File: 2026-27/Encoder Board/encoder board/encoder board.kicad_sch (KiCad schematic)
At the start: 7 parts, among them J1 jst-ph, U1 TLE5012BE1000

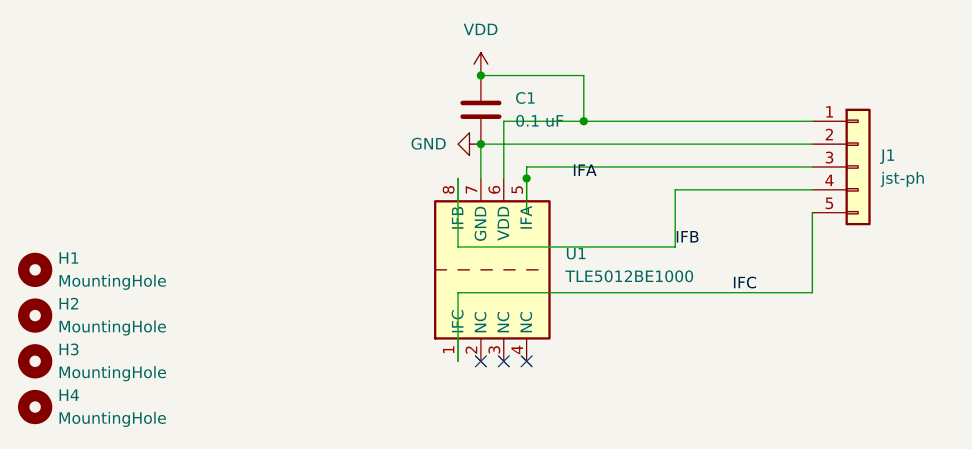
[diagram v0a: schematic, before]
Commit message: encoder board
designed encoder board to mechanical team's size specifications
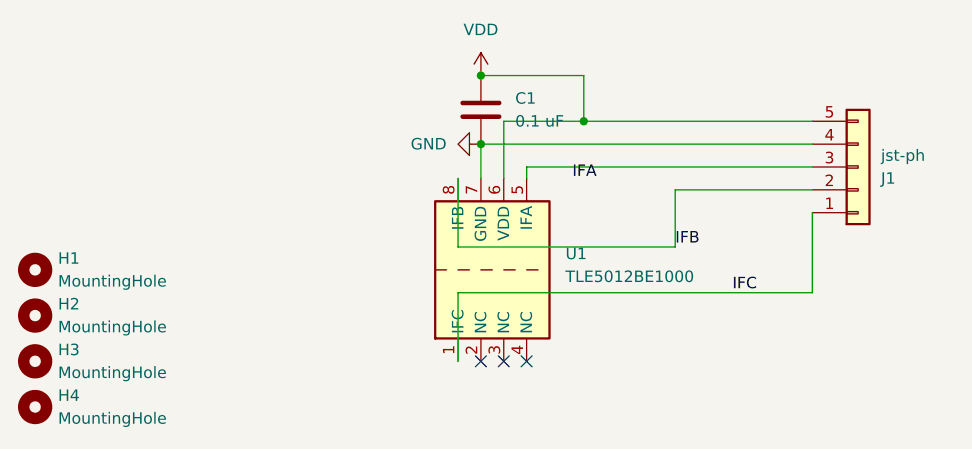
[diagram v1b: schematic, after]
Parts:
- H1, H2, H3, H4: footprint MountingHole:MountingHole_3.2mm_M3 -> MountingHole:MountingHole_2.7mm_M2.5
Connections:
- net GND: now also J1.4 (Pin_4); no longer J1.2 (Pin_2)
- net IFC: now also J1.1 (Pin_1); no longer J1.5 (Pin_5)
- net VDD: now also J1.2 (Pin_2), J1.5 (Pin_5); no longer J1.1 (Pin_1), J1.4 (Pin_4)
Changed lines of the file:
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@@
-		(color 0 0 0 0)
-	)
-	(junction
-		(at 135.89 58.42)
-		(diameter 0)
 		(color 0 0 0 0)
 	)
@@
 	(wire
 		(pts
-			(xy 135.89 58.42) (xy 135.89 57.15)
-		)
-		(stroke
-			(width 0)
-			(type default)
-		)
-	)
-	(wire
-		(pts
 			(xy 142.24 52.07) (xy 133.35 52.07)
 		)
@@
 	(wire
 		(pts
-			(xy 135.89 58.42) (xy 135.89 62.23)
+			(xy 135.89 57.15) (xy 135.89 58.42)
 		)
 		(stroke
@@
 			)
 		)
-		(property "Footprint" "MountingHole:MountingHole_3.2mm_M3"
+		(property "Footprint" "MountingHole:MountingHole_2.7mm_M2.5"
 			(at 81.28 68.58 0)
 			(hide yes)
@@
 	)
 	(symbol
+		(lib_id "Interface_CAN_LIN:ISO1044BD")
+		(at 130.81 68.58 90)
+		(unit 1)
+		(body_style 1)
+		(exclude_from_sim no)
+		(in_bom yes)
+		(on_board yes)
+		(in_pos_files yes)
+		(dnp no)
+		(property "Reference" "U1"
+			(at 140.208 66.802 90)
+			(show_name no)
+			(do_not_autoplace no)
+			(effects
+				(font
+					(size 1.27 1.27)
+				)
+				(justify right)
+			)
+		)
+		(property "Value" "TLE5012BE1000"
+			(at 140.208 69.342 90)
+			(show_name no)
+			(do_not_autoplace no)
+			(effects
+				(font
+					(size 1.27 1.27)
+				)
+				(justify right)
+			)
+		)
+		(property "Footprint" "Package_SO:SOIC-8_3.9x4.9mm_P1.27mm"
+			(at 140.97 68.58 0)
+			(hide yes)
+			(show_name no)
+			(do_not_autoplace no)
+			(effects
+				(font
+					(size 1.27 1.27)
+					(italic yes)
+				)
+			)
+		)
+		(property "Datasheet" "https://www.ti.com/lit/ds/symlink/iso1044.pdf"
+			(at 143.51 68.58 0)
+			(hide yes)
+			(show_name no)
+			(do_not_autoplace no)
+			(effects
+				(font
+					(size 1.27 1.27)
+				)
+			)
+		)
+		(property "Description" "angle sensor, SOIC-8"
+			(at 118.872 67.31 0)
+			(hide yes)
+			(show_name no)
+			(do_not_autoplace no)
+			(effects
+				(font
+					(size 1.27 1.27)
+				)
+			)
+		)
+		(pin "7"
+		)
+		(pin "4"
+		)
+		(pin "6"
+		)
+		(pin "1"
+		)
+		(pin "2"
+		)
+		(pin "8"
+		)
+		(pin "5"
+		)
+		(pin "3"
+		)
+		(instances
+			(project "encoder board"
+				(path "/4ad8da32-6a39-4fcb-82be-0e55f6dd2596"
+					(reference "U1")
+					(unit 1)
+				)
+			)
+		)
+	)
+	(symbol
 		(lib_id "Mechanical:MountingHole")
 		(at 81.28 73.66 0)
@@
 			)
 		)
-		(property "Footprint" "MountingHole:MountingHole_3.2mm_M3"
+		(property "Footprint" "MountingHole:MountingHole_2.7mm_M2.5"
 			(at 81.28 73.66 0)
 			(hide yes)
@@
 			)
 		)
-		(property "Footprint" "MountingHole:MountingHole_3.2mm_M3"
+		(property "Footprint" "MountingHole:MountingHole_2.7mm_M2.5"
 			(at 81.28 83.82 0)
 			(hide yes)
@@
 	)
 	(symbol
-		(lib_id "Connector_Generic:Conn_01x05")
-		(at 172.72 57.15 0)
-		(unit 1)
-		(body_style 1)
-		(exclude_from_sim no)
-		(in_bom yes)
-		(on_board yes)
-		(in_pos_files yes)
-		(dnp no)
-		(fields_autoplaced yes)
-		(property "Reference" "J1"
-			(at 175.26 55.8799 0)
-			(show_name no)
-			(do_not_autoplace no)
-			(effects
-				(font
-					(size 1.27 1.27)
-				)
-				(justify left)
-			)
-		)
-		(property "Value" "jst-ph"
-			(at 175.26 58.4199 0)
-			(show_name no)
-			(do_not_autoplace no)
-			(effects
-				(font
-					(size 1.27 1.27)
-				)
-				(justify left)
-			)
-		)
-		(property "Footprint" "Connector_JST:JST_PH_S5B-PH-K_1x05_P2.00mm_Horizontal"
-			(at 172.72 57.15 0)
-			(hide yes)
-			(show_name no)
-			(do_not_autoplace no)
-			(effects
-				(font
-					(size 1.27 1.27)
-				)
-			)
-		)
-		(property "Datasheet" ""
-			(at 172.72 57.15 0)
-			(hide yes)
-			(show_name no)
-			(do_not_autoplace no)
-			(effects
-				(font
-					(size 1.27 1.27)
-				)
-			)
-		)
-		(property "Description" "Generic connector, single row, 01x05, script generated (kicad-library-utils/schlib/autogen/connector/)"
-			(at 172.72 57.15 0)
-			(hide yes)
-			(show_name no)
-			(do_not_autoplace no)
-			(effects
-				(font
-					(size 1.27 1.27)
-				)
-			)
-		)
-		(pin "3"
-		)
-		(pin "1"
-		)
-		(pin "5"
-		)
-		(pin "4"
-		)
-		(pin "2"
-		)
-		(instances
-			(project "encoder board"
-				(path "/4ad8da32-6a39-4fcb-82be-0e55f6dd2596"
-					(reference "J1")
-					(unit 1)
-				)
-			)
-		)
-	)
-	(symbol
 		(lib_id "Device:C")
 		(at 130.81 50.8 0)
@@
 			)
 		)
-		(property "Footprint" "MountingHole:MountingHole_3.2mm_M3"
+		(property "Footprint" "MountingHole:MountingHole_2.7mm_M2.5"
 			(at 81.28 78.74 0)
 			(hide yes)
@@
 	)
 	(symbol
-		(lib_id "Interface_CAN_LIN:ISO1044BD")
-		(at 130.81 68.58 90)
+		(lib_id "Connector_Generic:Conn_01x05")
+		(at 172.72 57.15 0)
+		(mirror x)
 		(unit 1)
 		(body_style 1)
@@
 		(in_pos_files yes)
 		(dnp no)
-		(property "Reference" "U1"
-			(at 140.208 66.802 90)
-			(show_name no)
-			(do_not_autoplace no)
-			(effects
-				(font
-					(size 1.27 1.27)
-				)
-				(justify right)
-			)
-		)
-		(property "Value" "TLE5012BE1000"
-			(at 140.208 69.342 90)
-			(show_name no)
-			(do_not_autoplace no)
-			(effects
-				(font
-					(size 1.27 1.27)
-				)
-				(justify right)
-			)
-		)
-		(property "Footprint" "Package_SO:SOIC-8_3.9x4.9mm_P1.27mm"
-			(at 140.97 68.58 0)
-			(hide yes)
-			(show_name no)
-			(do_not_autoplace no)
-			(effects
-				(font
-					(size 1.27 1.27)
-					(italic yes)
-				)
-			)
-		)
-		(property "Datasheet" "https://www.ti.com/lit/ds/symlink/iso1044.pdf"
-			(at 143.51 68.58 0)
-			(hide yes)
-			(show_name no)
-			(do_not_autoplace no)
-			(effects
-				(font
-					(size 1.27 1.27)
-				)
-			)
-		)
-		(property "Description" "angle sensor, SOIC-8"
-			(at 118.872 67.31 0)
-			(hide yes)
-			(show_name no)
-			(do_not_autoplace no)
-			(effects
-				(font
-					(size 1.27 1.27)
-				)
-			)
-		)
-		(pin "7"
+		(property "Reference" "J1"
+			(at 175.26 58.4201 0)
+			(show_name no)
+			(do_not_autoplace no)
+			(effects
+				(font
+					(size 1.27 1.27)
+				)
+				(justify left)
+			)
+		)
+		(property "Value" "jst-ph"
+			(at 175.26 55.8801 0)
+			(show_name no)
+			(do_not_autoplace no)
+			(effects
+				(font
+					(size 1.27 1.27)
+				)
+				(justify left)
+			)
+		)
+		(property "Footprint" "Connector_JST:JST_PH_S5B-PH-K_1x05_P2.00mm_Horizontal"
+			(at 172.72 57.15 0)
+			(hide yes)
+			(show_name no)
+			(do_not_autoplace no)
+			(effects
+				(font
+					(size 1.27 1.27)
+				)
+			)
+		)
+		(property "Datasheet" ""
+			(at 172.72 57.15 0)
+			(hide yes)
+			(show_name no)
+			(do_not_autoplace no)
+			(effects
+				(font
+					(size 1.27 1.27)
+				)
+			)
+		)
+		(property "Description" "Generic connector, single row, 01x05, script generated (kicad-library-utils/schlib/autogen/connector/)"
+			(at 172.72 57.15 0)
+			(hide yes)
+			(show_name no)
+			(do_not_autoplace no)
+			(effects
+				(font
+					(size 1.27 1.27)
+				)
+			)
+		)
+		(pin "3"
+		)
+		(pin "1"
+		)
+		(pin "5"
 		)
 		(pin "4"
 		)
-		(pin "6"
-		)
-		(pin "1"
-		)
 		(pin "2"
-		)
-		(pin "8"
-		)
-		(pin "5"
-		)
-		(pin "3"
 		)
 		(instances
 			(project "encoder board"
 				(path "/4ad8da32-6a39-4fcb-82be-0e55f6dd2596"
-					(reference "U1")
+					(reference "J1")
 					(unit 1)
 				)
